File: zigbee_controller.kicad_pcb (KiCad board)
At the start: 2 copper layers, 55.5 x 64.4 mm, 78 parts, among them J1 KF635, J10 TerminalBlock_KF301-5.0, J11 TerminalBlock_KF301-5.0, J12 TerminalBlock_KF301-5.0, J13 TerminalBlock_KF301-5.0, J3 Conn_01x06, J4 Conn_01x07, J5 Conn_01x05, P1 USB_C_Receptacle_GCT_USB4105, Q2 IRLB3813, Q3 IRLB3813, Q4 IRLB3813, Q5 IRLB3813, SW2 EN, SW4 Boot, U1 TPS54560, U2 ESP32-C6-MINI-1, U4 TC4427, U5 TC4427, U6 RT9080, U9 CH224K

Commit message: Clarify disconnecting before attaching USB
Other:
- board text added: "- 2oz copper - U1: TPS54560 - U4/U5: TC4427 - U6: RT9080 - U9: CH224K - D1: B650C - J1: KF635 - Q2-Q5: IRLB3813 - SW1/SW2: 3x4x2 switch - L1: 1040 10μH inductor 0530 - J10-J13: KF301-5.0 - D4-D7: Optional fly-back diode MBRB2045CT (Schottky) - D2/D3 LESD5D5.0CT1G"
- board text added: "When terminal power is bridged, disconnect everything before connecting USB"
- board text removed: "- 2oz copper - U1: TPS54560 - U4/U5: TC4427 - U6: XT9080 - U9: CH224K - D1: B650C - J1: KF635 - Q2-Q5: IRLB3813 - SW1/SW2: 3x4x2 switch - L1: 1040 10μH inductor 0530 - J10-J13: KF301-5.0 - D4-D7: Optional fly-back diode MBRB2045CT (Schottky) - D2/D3 LESD5D5.0CT1G"
- board text removed: "Do not connect USB, when powering via the terminal"

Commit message: Clarify only connect USB or terminal pads
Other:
- board text added: "Connect either terminal or USB power pads"
- board text removed: "Never bridge terminal and USB power pads"

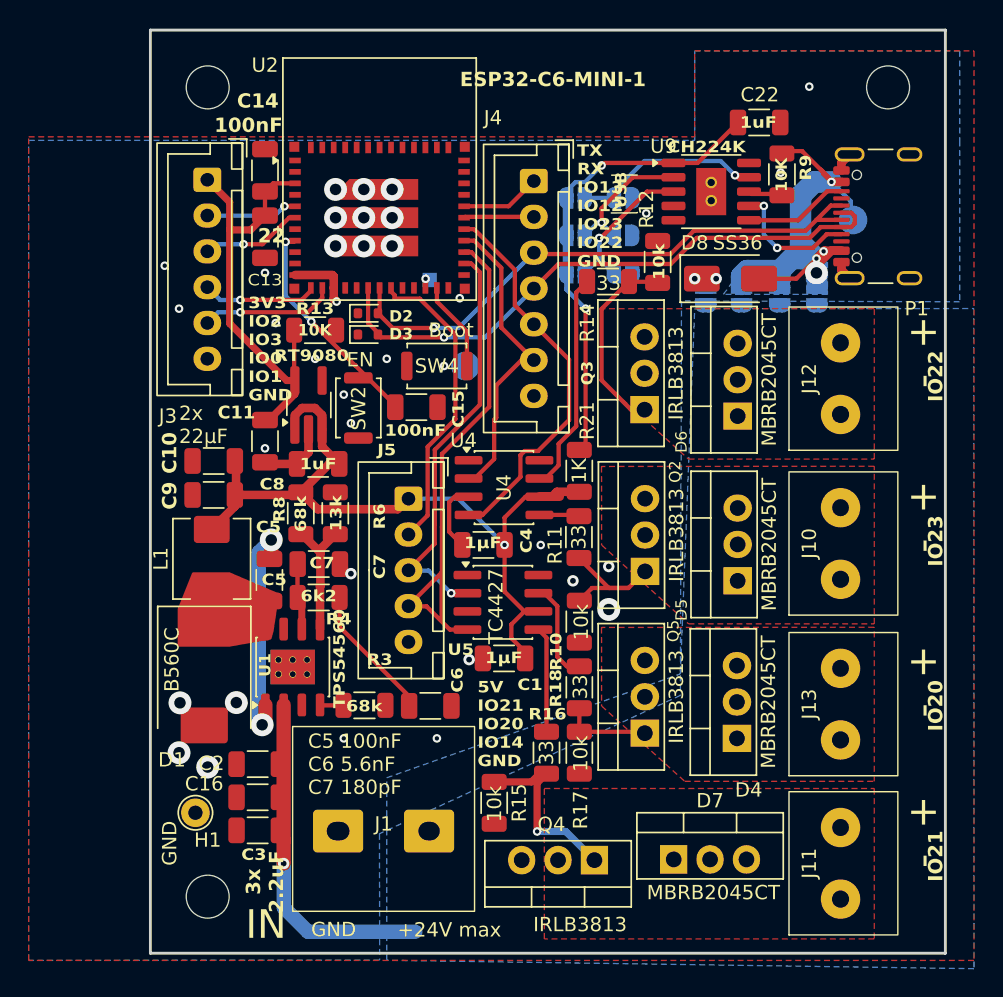
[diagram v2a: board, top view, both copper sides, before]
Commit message: two diods for USB powering when in terminal mode
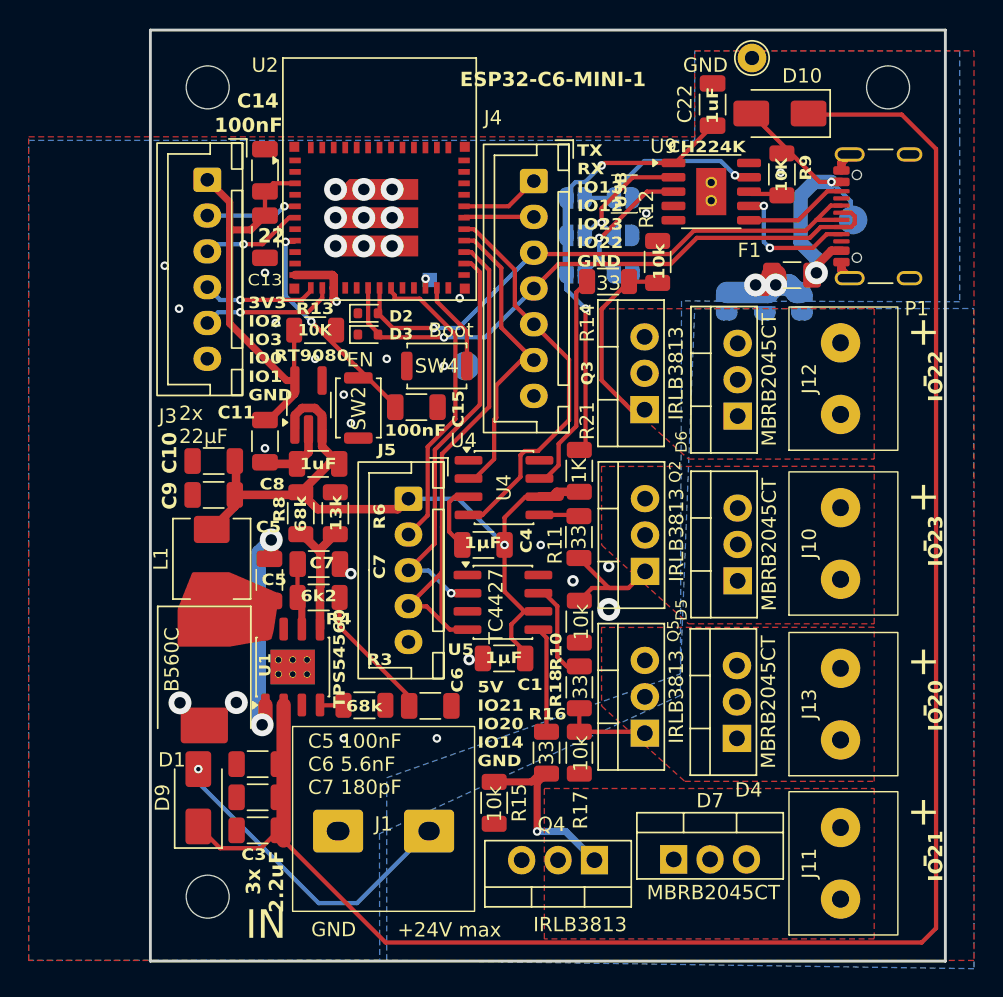
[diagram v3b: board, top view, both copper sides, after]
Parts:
- removed D8: SS36, Diode_SMD:D_SMA
- removed JP8: Terminal power, Jumper:SolderJumper-2_P1.3mm_Open_RoundedPad1.0x1.5mm
- added D10: SS14, Diode_SMD:D_SMA, F.Cu at (196.4, 74.3)
- added D9: SS14, Diode_SMD:D_SMA, F.Cu at (155.8, 122.1)
- added F1: Fuse, Fuse:Fuse_1206_3216Metric, F.Cu at (197.3, 85.6)
- moved TP3 65.5 mm to (194.5, 70.5)
- moved C22 3.48 mm to (191.8, 73.7), turned to 90 degrees
- moved JP10 1.18 mm to (198.0, 87.6)
- moved JP9 1.18 mm to (195.4, 87.6)
- moved JP7 1.18 mm to (192.7, 87.6)
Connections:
- C16 pad 1: +24V -> Net-(D10-K)
- C2 pad 1: +24V -> Net-(D10-K)
- C3 pad 1: +24V -> Net-(D10-K)
- JP10 pad 2: VBUS -> Net-(JP10-B)
- JP7 pad 2: VBUS -> Net-(JP10-B)
- JP9 pad 2: VBUS -> Net-(JP10-B)
- U1 pad 2: +24V -> Net-(D10-K)
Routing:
- net Net-(D10-K): track 0.00 -> 129.4 mm
- net VBUS: track 37.3 -> 24.9 mm, vias 4 -> 2
- net Net-(JP10-B): track 0.00 -> 8.08 mm, vias 0 -> 2
- net /CH224k_Vdd: track 31.6 -> 29.6 mm
- net Net-(D8-K): track 1.96 -> 0.00 mm, vias 2 -> 0
- net +24V: track 24.0 -> 22.6 mm
- net GND: vias 36 -> 33
- removed copper zone on B.Cu, net VBUS
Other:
- board size 55.5 x 64.4 mm -> 55.5 x 65 mm

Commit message: USB powering via 3A or 5A fuse
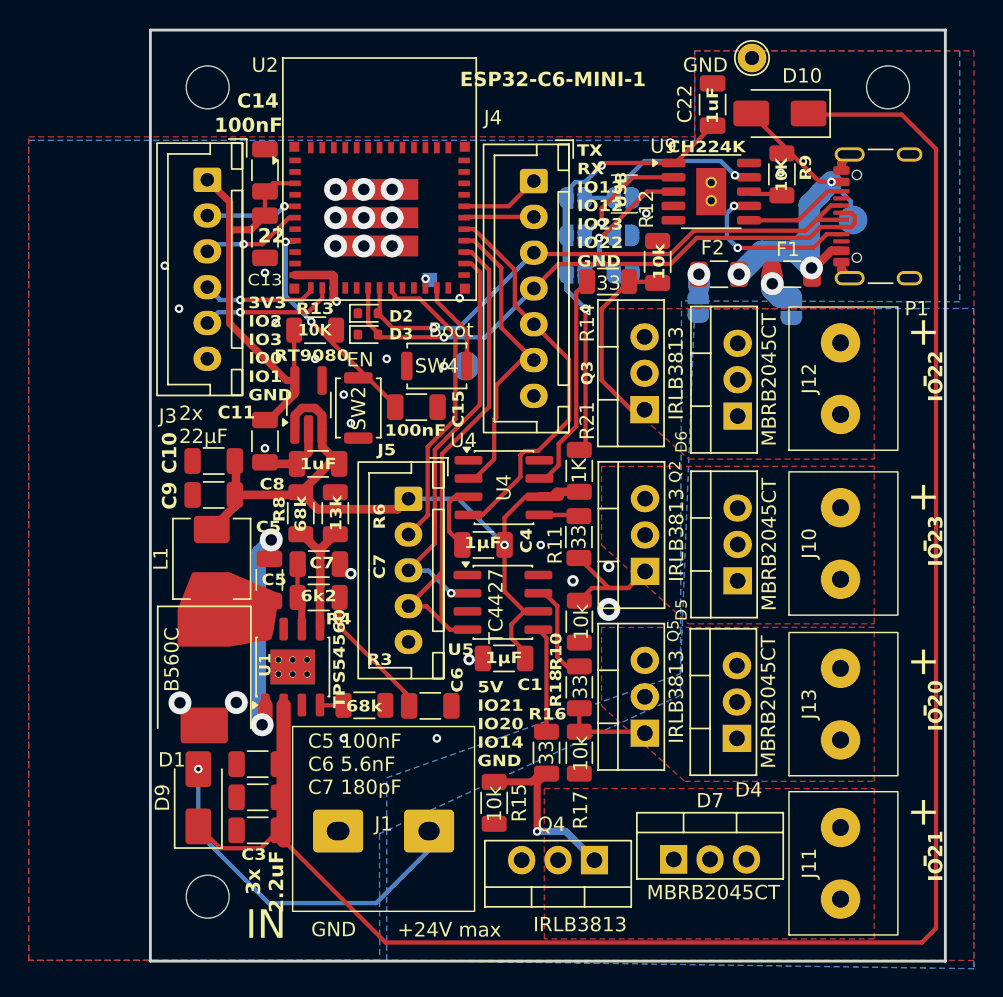
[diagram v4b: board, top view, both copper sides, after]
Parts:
- removed JP9: power_via_usb, Jumper:SolderJumper-2_P1.3mm_Open_RoundedPad1.0x1.5mm
- added F2: Fuse 3A, Fuse:Fuse_1206_3216Metric, F.Cu at (192.2, 85.5)
- F1: value Fuse -> Fuse 5A
- JP10: value power_via_usb -> USB power 3A
- JP7: value power_via_usb -> USB power 5A
- moved JP10 7.24 mm to (190.8, 87.8)
- moved JP7 4.53 mm to (197.2, 88.0)
- moved F1 0.07 mm to (197.3, 85.5)
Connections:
- F1 pad 2: Net-(JP10-B) -> Net-(JP7-B)
- JP7 pad 2: Net-(JP10-B) -> Net-(JP7-B)
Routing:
- net Net-(JP10-B): track 8.08 -> 0.92 mm, vias 2 -> 1
- net VBUS: track 24.9 -> 30.3 mm, vias 2 -> 3
- net Net-(JP7-B): track 0.00 -> 3.02 mm, vias 0 -> 1
- net +24V: track 22.6 -> 25.4 mm
- net /CC1: track 9.53 -> 12.1 mm
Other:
- board text removed: "Connect either terminal or USB power pads"
- board text removed: "USB power"
- board text removed: "When terminal power is bridged, disconnect everything before connecting USB"

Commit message: Add ground to buck
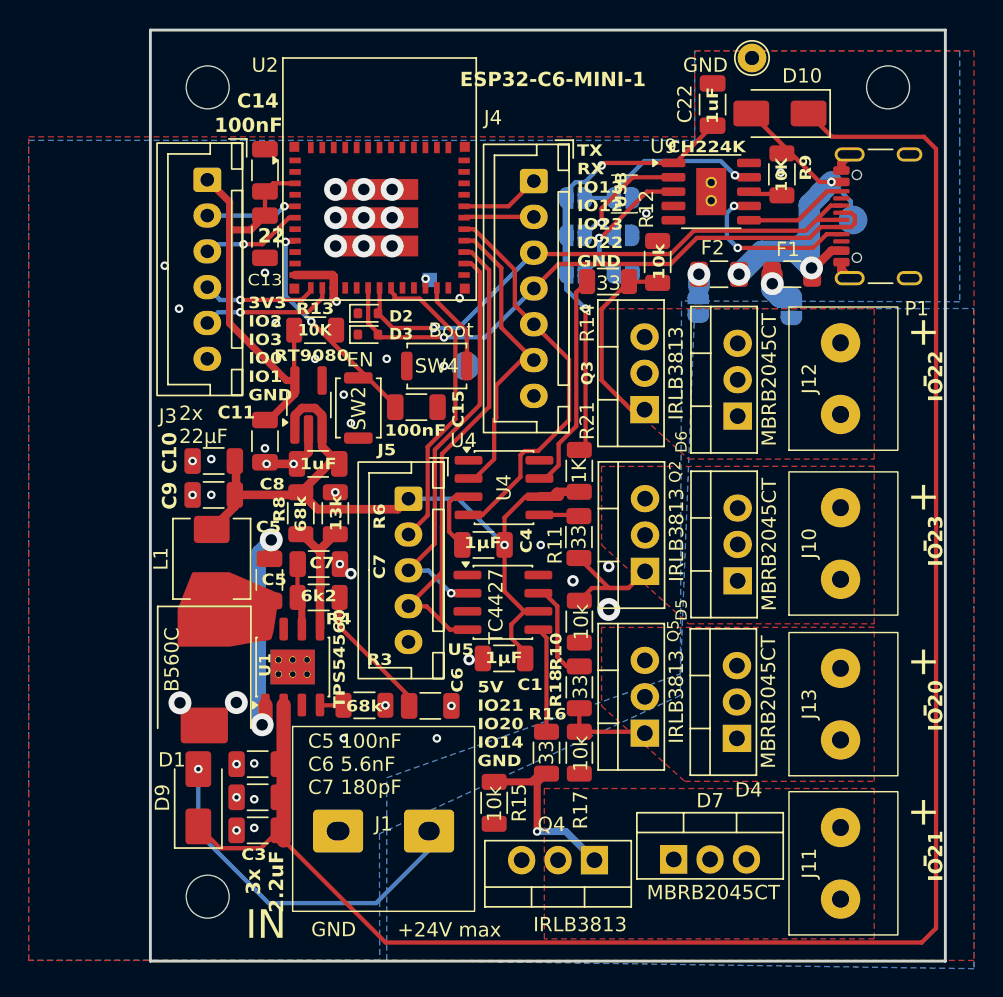
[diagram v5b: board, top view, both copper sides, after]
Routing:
- net GND: vias 33 -> 49
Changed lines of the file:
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@@
+	)
+	(segment
+		(start 162.5 98.787388)
+		(end 160.612388 98.787388)
+		(width 0.6)
+		(layer "F.Cu")
+		(net "GND")
 	)
 	(segment
@@
 	(segment
 		(start 162.735054 98.787388)
-		(end 160.612388 98.787388)
+		(end 162.5 98.787388)
 		(width 0.6)
 		(layer "F.Cu")
@@
 	)
 	(via
+		(at 159.75 119.7)
+		(size 0.6)
+		(drill 0.3)
+		(layers "F.Cu" "B.Cu")
+		(free yes)
+		(net "GND")
+	)
+	(via
 		(at 196.5 78.45)
 		(size 0.6)
@@
 	)
 	(via
+		(at 162.5 98.787388)
+		(size 0.6)
+		(drill 0.3)
+		(layers "F.Cu" "B.Cu")
+		(net "GND")
+	)
+	(via
 		(at 173 91.95)
+		(size 0.6)
+		(drill 0.3)
+		(layers "F.Cu" "B.Cu")
+		(net "GND")
+	)
+	(via
+		(at 158.513993 124.370072)
 		(size 0.6)
 		(drill 0.3)
@@
 	)
 	(via
+		(at 160.612388 98.787388)
+		(size 0.6)
+		(drill 0.3)
+		(layers "F.Cu" "B.Cu")
+		(net "GND")
+	)
+	(via
 		(at 174.75 112.45)
 		(size 0.8)
@@
 	)
 	(via
+		(at 173.515767 115.680825)
+		(size 0.6)
+		(drill 0.3)
+		(layers "F.Cu" "B.Cu")
+		(net "GND")
+	)
+	(via
+		(at 158.513993 119.747461)
+		(size 0.6)
+		(drill 0.3)
+		(layers "F.Cu" "B.Cu")
+		(net "GND")
+	)
+	(via
 		(at 166.5 106.45)
 		(size 0.8)
@@
 	)
 	(via
+		(at 159.75 122.2)
+		(size 0.6)
+		(drill 0.3)
+		(layers "F.Cu" "B.Cu")
+		(free yes)
+		(net "GND")
+	)
+	(via
 		(at 154.564756 115.467605)
 		(size 1.6)
@@
 	)
 	(via
+		(at 158.513993 122.062203)
+		(size 0.6)
+		(drill 0.3)
+		(layers "F.Cu" "B.Cu")
+		(net "GND")
+	)
+	(via
 		(at 187.118462 81.296874)
 		(size 0.6)
@@
 		(layers "F.Cu" "B.Cu")
 		(free yes)
+		(net "GND")
+	)
+	(via
+		(at 168.906199 115.64304)
+		(size 0.6)
+		(drill 0.3)
+		(layers "F.Cu" "B.Cu")
 		(net "GND")
 	)
@@
 	)
 	(via
+		(at 165.730952 105.779616)
+		(size 0.6)
+		(drill 0.3)
+		(layers "F.Cu" "B.Cu")
+		(net "GND")
+	)
+	(via
+		(at 155.446028 98.585049)
+		(size 0.6)
+		(drill 0.3)
+		(layers "F.Cu" "B.Cu")
+		(net "GND")
+	)
+	(via
 		(at 167.4 79.625)
 		(size 1.6)
@@
 	)
 	(via
+		(at 156.75 98.45)
+		(size 0.6)
+		(drill 0.3)
+		(layers "F.Cu" "B.Cu")
+		(free yes)
+		(net "GND")
+	)
+	(via
 		(at 169.375 83.575)
 		(size 1.6)
@@
 	)
 	(via
+		(at 156.75 100.95)
+		(size 0.6)
+		(drill 0.3)
+		(layers "F.Cu" "B.Cu")
+		(free yes)
+		(net "GND")
+	)
+	(via
 		(at 179.75 104.45)
 		(size 0.6)
@@
 	)
 	(via
+		(at 165.408194 100.769507)
+		(size 0.6)
+		(drill 0.3)
+		(layers "F.Cu" "B.Cu")
+		(net "GND")
+	)
+	(via
+		(at 159.75 124.2)
+		(size 0.6)
+		(drill 0.3)
+		(layers "F.Cu" "B.Cu")
+		(free yes)
+		(net "GND")
+	)
+	(via
+		(at 155.443115 100.954908)
+		(size 0.6)
+		(drill 0.3)
+		(layers "F.Cu" "B.Cu")
+		(net "GND")
+	)
+	(via
 		(at 165.425 81.6)
 		(size 1.6)
@@
 	)
 	(segment
-		(start 204.95 74.4)
-		(end 207.35 76.8)
+		(start 168.921162 132.2)
+		(end 161.802588 125.081426)
 		(width 0.3)
 		(layer "F.Cu")
@@
 	)
 	(segment
+		(start 198.52298 74.4)
+		(end 200.07298 75.95)
+		(width 0.3)
+		(layer "F.Cu")
+		(net "Net-(D10-K)")
+	)
+	(segment
+		(start 207.35 76.8)
+		(end 207.35 131.2)
+		(width 0.3)
+		(layer "F.Cu")
+		(net "Net-(D10-K)")
+	)
+	(segment
+		(start 206.5 75.95)
+		(end 207.35 76.8)
+		(width 0.3)
+		(layer "F.Cu")
+		(net "Net-(D10-K)")
+	)
+	(segment
+		(start 160.213993 125.620072)
+		(end 161.463993 124.370072)
+		(width 0.3)
+		(layer "F.Cu")
+		(net "Net-(D10-K)")
+	)
+	(segment
+		(start 206.35 132.2)
+		(end 168.921162 132.2)
+		(width 0.3)
+		(layer "F.Cu")
+		(net "Net-(D10-K)")
+	)
+	(segment
+		(start 155.844764 124.094813)
+		(end 157.370023 125.620072)
+		(width 0.3)
+		(layer "F.Cu")
+		(net "Net-(D10-K)")
+	)
+	(segment
+		(start 157.370023 125.620072)
+		(end 160.213993 125.620072)
+		(width 0.3)
+		(layer "F.Cu")
+		(net "Net-(D10-K)")
+	)
+	(segment
 		(start 207.35 131.2)
 		(end 206.35 132.2)
@@
 	)
 	(segment
-		(start 206.35 132.2)
-		(end 168.921162 132.2)
-		(width 0.3)
-		(layer "F.Cu")
-		(net "Net-(D10-K)")
-	)
-	(segment
-		(start 160.213993 125.620072)
-		(end 161.463993 124.370072)
-		(width 0.3)
-		(layer "F.Cu")
-		(net "Net-(D10-K)")
-	)
-	(segment
-		(start 168.921162 132.2)
-		(end 161.802588 125.081426)
-		(width 0.3)
-		(layer "F.Cu")
-		(net "Net-(D10-K)")
-	)
-	(segment
-		(start 155.844764 124.094813)
-		(end 157.370023 125.620072)
-		(width 0.3)
-		(layer "F.Cu")
-		(net "Net-(D10-K)")
-	)
-	(segment
-		(start 198.52298 74.4)
-		(end 204.95 74.4)
-		(width 0.3)
-		(layer "F.Cu")
-		(net "Net-(D10-K)")
-	)
-	(segment
-		(start 157.370023 125.620072)
-		(end 160.213993 125.620072)
-		(width 0.3)
-		(layer "F.Cu")
-		(net "Net-(D10-K)")
-	)
-	(segment
-		(start 207.35 76.8)
-		(end 207.35 131.2)
-		(width 0.3)
-		(layer "F.Cu")
+		(start 200.07298 75.95)
+		(end 206.5 75.95)
+		(width 0.3)
+		(layer "F.Cu")

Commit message: Adapt instructions and dimensions.
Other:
- board text added: "To power from USB, bridge one of the two USB power pads. 5A only for 20v. Choose the voltage with the 6 CFG pads."
- board text removed: "To power from the IN terminal, bridge terminal power pad To power from USB, bridge the three USB power pad In USB-mode choose the voltage with the 6 CFG pads"

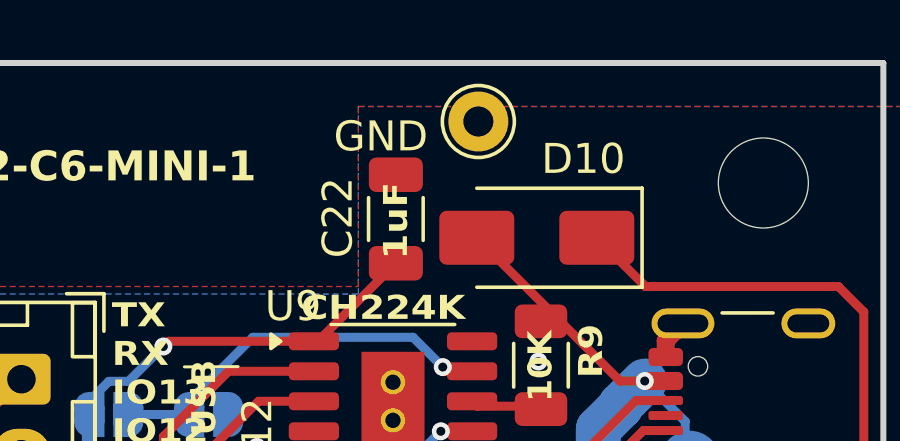
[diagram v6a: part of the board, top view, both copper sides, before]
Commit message: Move GND probe point
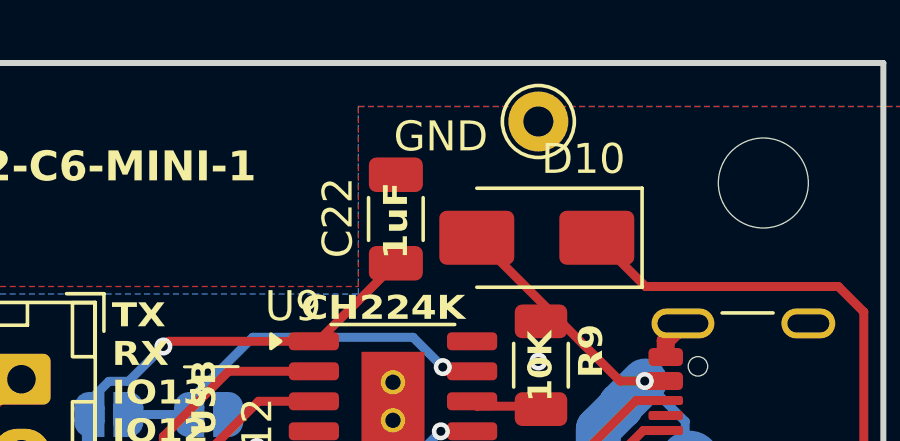
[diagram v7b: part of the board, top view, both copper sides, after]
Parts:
- moved TP3 2.00 mm to (196.5, 70.5)
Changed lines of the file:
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@@
 	(footprint "TestPoint:TestPoint_THTPad_D2.0mm_Drill1.0mm"
 		(layer "F.Cu")
-		(at 194.5 70.45)
+		(at 196.5 70.45)
 		(descr "THT pad as test Point, diameter 2.0mm, hole diameter 1.0mm")
 		(tags "test point THT pad")
